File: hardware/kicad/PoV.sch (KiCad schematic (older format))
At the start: 10 parts, among them SW1 SW_DPDT_x2, U1 ATtiny85-20PU

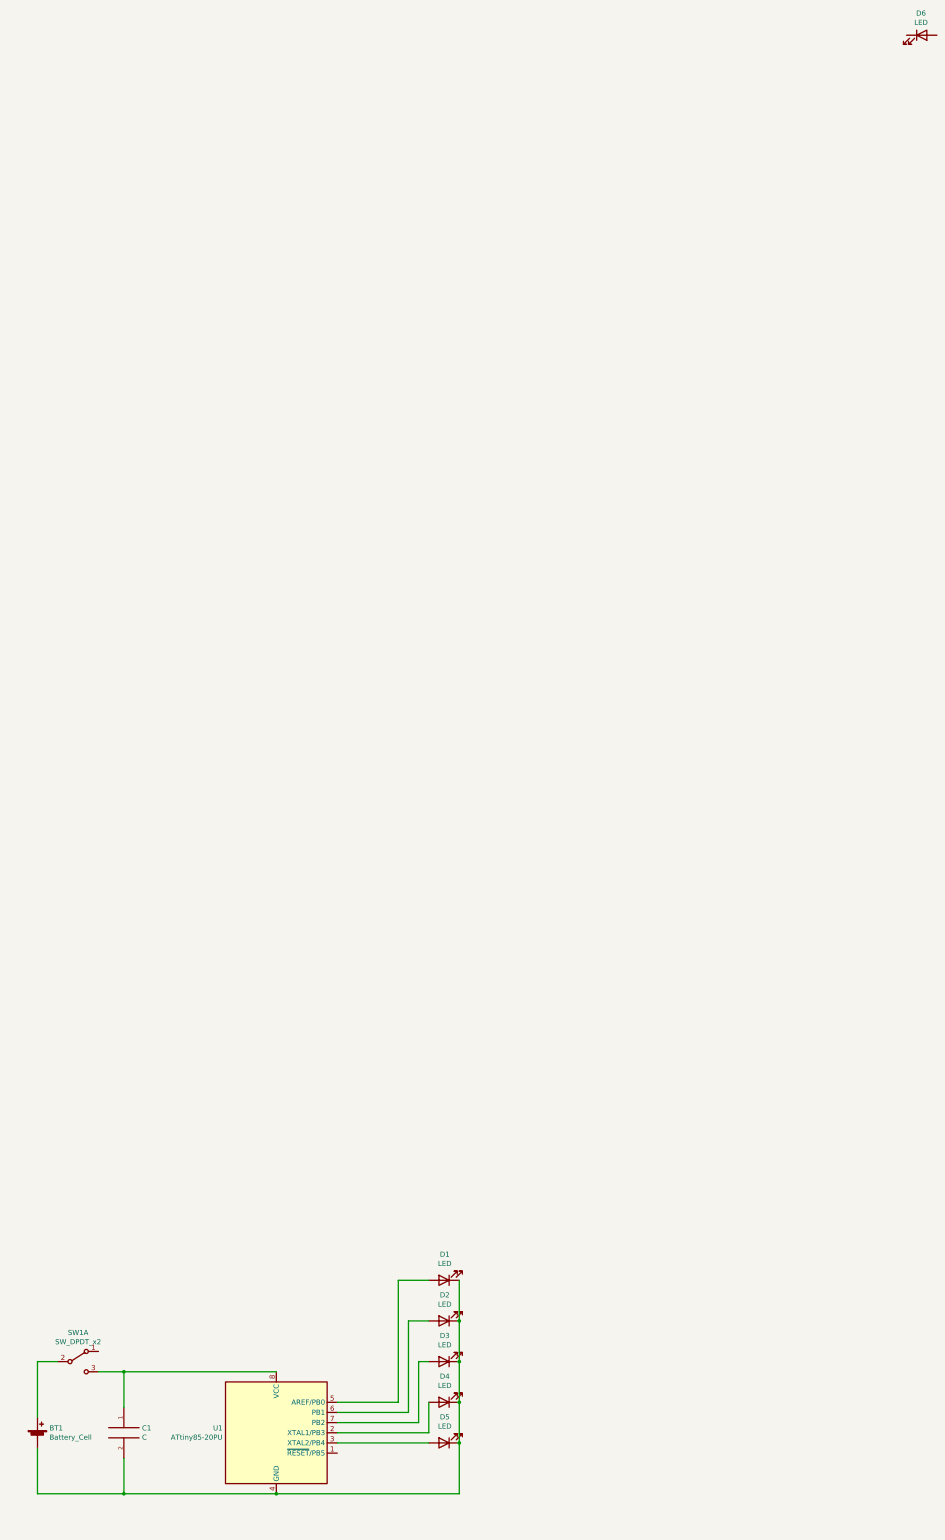
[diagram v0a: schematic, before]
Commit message: updated kicad schematic
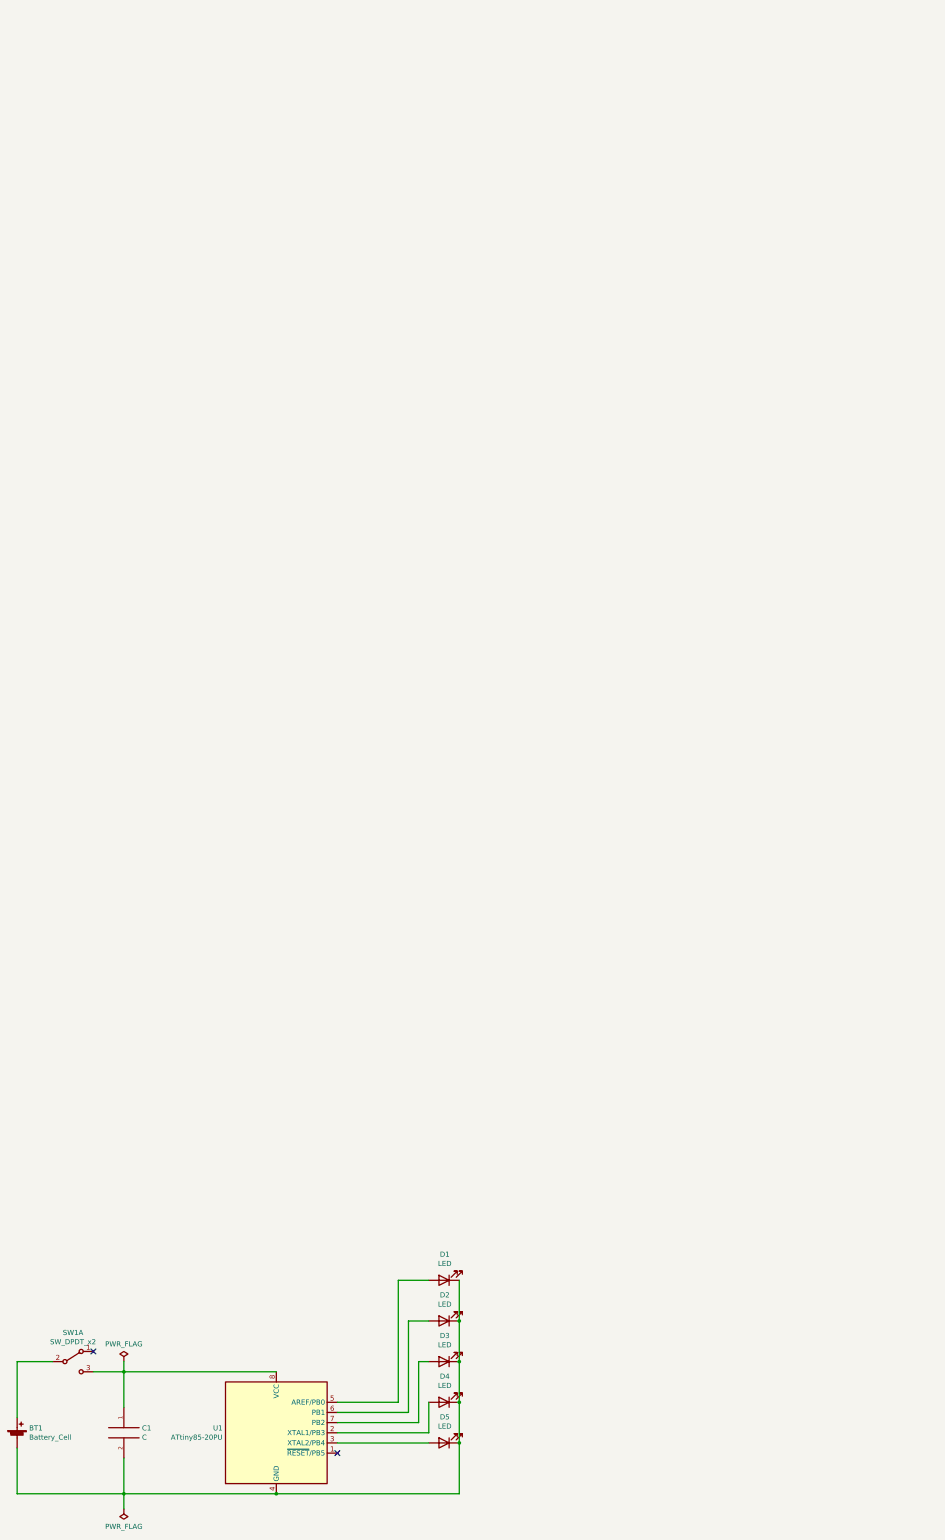
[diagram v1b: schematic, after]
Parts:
- removed D6: LED, symbol Device:LED
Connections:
- no-connect marks 0 -> 2
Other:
- moved on the sheet: BT1, SW1A
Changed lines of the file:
@@
-$EndComp
-$Comp
-L Device:LED D6
-U 1 1 6151B918
-P 12350 -9750
-F 0 "D6" H 12343 -9534 50  0000 C CNN
-F 1 "LED" H 12343 -9625 50  0000 C CNN
-F 2 "" H 12350 -9750 50  0001 C CNN
-F 3 "~" H 12350 -9750 50  0001 C CNN
-	1    12350 -9750
-	1    0    0    -1
 $EndComp
 $Comp
@@
 L Device:Battery_Cell BT1
 U 1 1 61526F5A
-P 3650 4050
-F 0 "BT1" H 3768 4146 50  0000 L CNN
-F 1 "Battery_Cell" H 3768 4055 50  0000 L CNN
-F 2 "" V 3650 4110 50  0001 C CNN
-F 3 "~" V 3650 4110 50  0001 C CNN
-	1    3650 4050
+P 3450 4050
+F 0 "BT1" H 3568 4146 50  0000 L CNN
+F 1 "Battery_Cell" H 3568 4055 50  0000 L CNN
+F 2 "" V 3450 4110 50  0001 C CNN
+F 3 "~" V 3450 4110 50  0001 C CNN
+	1    3450 4050
 	1    0    0    -1
 $EndComp
@@
 Wire Wire Line
 	4500 4600 4500 4250
-Wire Wire Line
-	3650 4150 3650 4600
-Wire Wire Line
-	3650 4600 4500 4600
-Connection ~ 4500 4600
 Wire Wire Line
 	6600 4100 7500 4100
@@
 L Switch:SW_DPDT_x2 SW1
 U 1 1 6154A9DE
-P 4050 3300
-F 0 "SW1" H 4050 3585 50  0000 C CNN
-F 1 "SW_DPDT_x2" H 4050 3494 50  0000 C CNN
-F 2 "" H 4050 3300 50  0001 C CNN
-F 3 "~" H 4050 3300 50  0001 C CNN
-	1    4050 3300
+P 4000 3300
+F 0 "SW1" H 4000 3585 50  0000 C CNN
+F 1 "SW_DPDT_x2" H 4000 3494 50  0000 C CNN
+F 2 "" H 4000 3300 50  0001 C CNN
+F 3 "~" H 4000 3300 50  0001 C CNN
+	1    4000 3300
+	1    0    0    -1
+$EndComp
+Connection ~ 4500 3400
+NoConn ~ 4200 3200
+NoConn ~ 6600 4200
+$Comp
+L power:PWR_FLAG #FLG0101
+U 1 1 6155DBBA
+P 4500 3300
+F 0 "#FLG0101" H 4500 3375 50  0001 C CNN
+F 1 "PWR_FLAG" H 4500 3473 50  0000 C CNN
+F 2 "" H 4500 3300 50  0001 C CNN
+F 3 "~" H 4500 3300 50  0001 C CNN
+	1    4500 3300
 	1    0    0    -1
 $EndComp
 Wire Wire Line
-	3850 3300 3650 3300
+	4500 4600 3450 4600
 Wire Wire Line
-	3650 3300 3650 3850
+	3450 4600 3450 4150
+Connection ~ 4500 4600
 Wire Wire Line
-	4250 3400 4500 3400
-Connection ~ 4500 3400
+	3450 3850 3450 3300
+Wire Wire Line
+	4500 3300 4500 3400
+Wire Wire Line
+	4500 3400 4200 3400
+Wire Wire Line
+	3800 3300 3450 3300
+$Comp
+L power:PWR_FLAG #FLG0102
+U 1 1 6156979C
+P 4500 4750
+F 0 "#FLG0102" H 4500 4825 50  0001 C CNN
+F 1 "PWR_FLAG" H 4500 4923 50  0000 C CNN
+F 2 "" H 4500 4750 50  0001 C CNN
+F 3 "~" H 4500 4750 50  0001 C CNN
+	1    4500 4750
+	-1   0    0    1
+$EndComp
+Wire Wire Line
+	4500 4600 4500 4750
 $EndSCHEMATC

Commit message: woking on kicad
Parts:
- BT1: footprint (none) -> Battery:BatteryHolder_Keystone_103_1x20mm
- C1: footprint (none) -> Capacitor_THT:C_Disc_D3.0mm_W1.6mm_P2.50mm
- D1, D2, D3, D4, D5: footprint (none) -> LED_THT:LED_D5.0mm
- SW1: footprint (none) -> Button_Switch_THT:SW_CuK_JS202011AQN_DPDT_Angled
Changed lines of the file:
@@
 EESchema Schematic File Version 4
+LIBS:PoV-cache
 EELAYER 30 0
 EELAYER END
@@
 F 0 "D1" H 7643 2245 50  0000 C CNN
 F 1 "LED" H 7643 2336 50  0000 C CNN
-F 2 "" H 7650 2500 50  0001 C CNN
+F 2 "LED_THT:LED_D5.0mm" H 7650 2500 50  0001 C CNN
 F 3 "~" H 7650 2500 50  0001 C CNN
 	1    7650 2500
@@
 F 0 "D2" H 7643 2645 50  0000 C CNN
 F 1 "LED" H 7643 2736 50  0000 C CNN
-F 2 "" H 7650 2900 50  0001 C CNN
+F 2 "LED_THT:LED_D5.0mm" H 7650 2900 50  0001 C CNN
 F 3 "~" H 7650 2900 50  0001 C CNN
 	1    7650 2900
@@
 F 0 "D3" H 7643 3045 50  0000 C CNN
 F 1 "LED" H 7643 3136 50  0000 C CNN
-F 2 "" H 7650 3300 50  0001 C CNN
+F 2 "LED_THT:LED_D5.0mm" H 7650 3300 50  0001 C CNN
 F 3 "~" H 7650 3300 50  0001 C CNN
 	1    7650 3300
@@
 F 0 "D4" H 7643 3445 50  0000 C CNN
 F 1 "LED" H 7643 3536 50  0000 C CNN
-F 2 "" H 7650 3700 50  0001 C CNN
+F 2 "LED_THT:LED_D5.0mm" H 7650 3700 50  0001 C CNN
 F 3 "~" H 7650 3700 50  0001 C CNN
 	1    7650 3700
@@
 F 0 "D5" H 7643 3845 50  0000 C CNN
 F 1 "LED" H 7643 3936 50  0000 C CNN
-F 2 "" H 7650 4100 50  0001 C CNN
+F 2 "LED_THT:LED_D5.0mm" H 7650 4100 50  0001 C CNN
 F 3 "~" H 7650 4100 50  0001 C CNN
 	1    7650 4100
@@
 F 0 "BT1" H 3568 4146 50  0000 L CNN
 F 1 "Battery_Cell" H 3568 4055 50  0000 L CNN
-F 2 "" V 3450 4110 50  0001 C CNN
+F 2 "Battery:BatteryHolder_Keystone_103_1x20mm" V 3450 4110 50  0001 C CNN
 F 3 "~" V 3450 4110 50  0001 C CNN
 	1    3450 4050
@@
 F 0 "C1" H 4678 4046 50  0000 L CNN
 F 1 "C" H 4678 3955 50  0000 L CNN
-F 2 "" H 4500 4000 50  0001 C CNN
+F 2 "Capacitor_THT:C_Disc_D3.0mm_W1.6mm_P2.50mm" H 4500 4000 50  0001 C CNN
 F 3 "~" H 4500 4000 50  0001 C CNN
 	1    4500 4000
@@
 F 0 "SW1" H 4000 3585 50  0000 C CNN
 F 1 "SW_DPDT_x2" H 4000 3494 50  0000 C CNN
-F 2 "" H 4000 3300 50  0001 C CNN
+F 2 "Button_Switch_THT:SW_CuK_JS202011AQN_DPDT_Angled" H 4000 3300 50  0001 C CNN
 F 3 "~" H 4000 3300 50  0001 C CNN
 	1    4000 3300

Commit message: added first schematic draw
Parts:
- U1: symbol MCU_Microchip_ATtiny:ATtiny85-20PU -> PoV-rescue:ATtiny85-20PU-MCU_Microchip_ATtiny
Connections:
- net at C1.1, U1.8 (VCC): now also SW1.2 (B); no longer SW1.3 (C)
- net at BT1.1 (+): now also SW1.3 (C); no longer SW1.2 (B)
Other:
- moved on the sheet: SW1A
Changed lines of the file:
@@
 EESchema Schematic File Version 4
-LIBS:PoV-cache
 EELAYER 30 0
 EELAYER END
@@
 $EndDescr
 $Comp
-L MCU_Microchip_ATtiny:ATtiny85-20PU U1
+L PoV-rescue:ATtiny85-20PU-MCU_Microchip_ATtiny U1
 U 1 1 6151AF9F
 P 6000 4000
@@
 L Switch:SW_DPDT_x2 SW1
 U 1 1 6154A9DE
-P 4000 3300
-F 0 "SW1" H 4000 3585 50  0000 C CNN
-F 1 "SW_DPDT_x2" H 4000 3494 50  0000 C CNN
-F 2 "Button_Switch_THT:SW_CuK_JS202011AQN_DPDT_Angled" H 4000 3300 50  0001 C CNN
-F 3 "~" H 4000 3300 50  0001 C CNN
-	1    4000 3300
-	1    0    0    -1
+P 4000 3400
+F 0 "SW1" H 4000 3685 50  0000 C CNN
+F 1 "SW_DPDT_x2" H 4000 3594 50  0000 C CNN
+F 2 "Button_Switch_THT:SW_CuK_JS202011AQN_DPDT_Angled" H 4000 3400 50  0001 C CNN
+F 3 "~" H 4000 3400 50  0001 C CNN
+	1    4000 3400
+	-1   0    0    1
 $EndComp
 Connection ~ 4500 3400
@@
 Wire Wire Line
 	4500 3300 4500 3400
-Wire Wire Line
-	4500 3400 4200 3400
-Wire Wire Line
-	3800 3300 3450 3300
 $Comp
 L power:PWR_FLAG #FLG0102
@@
 Wire Wire Line
 	4500 4600 4500 4750
+Wire Wire Line
+	4200 3400 4500 3400
+Wire Wire Line
+	3450 3300 3800 3300
 $EndSCHEMATC

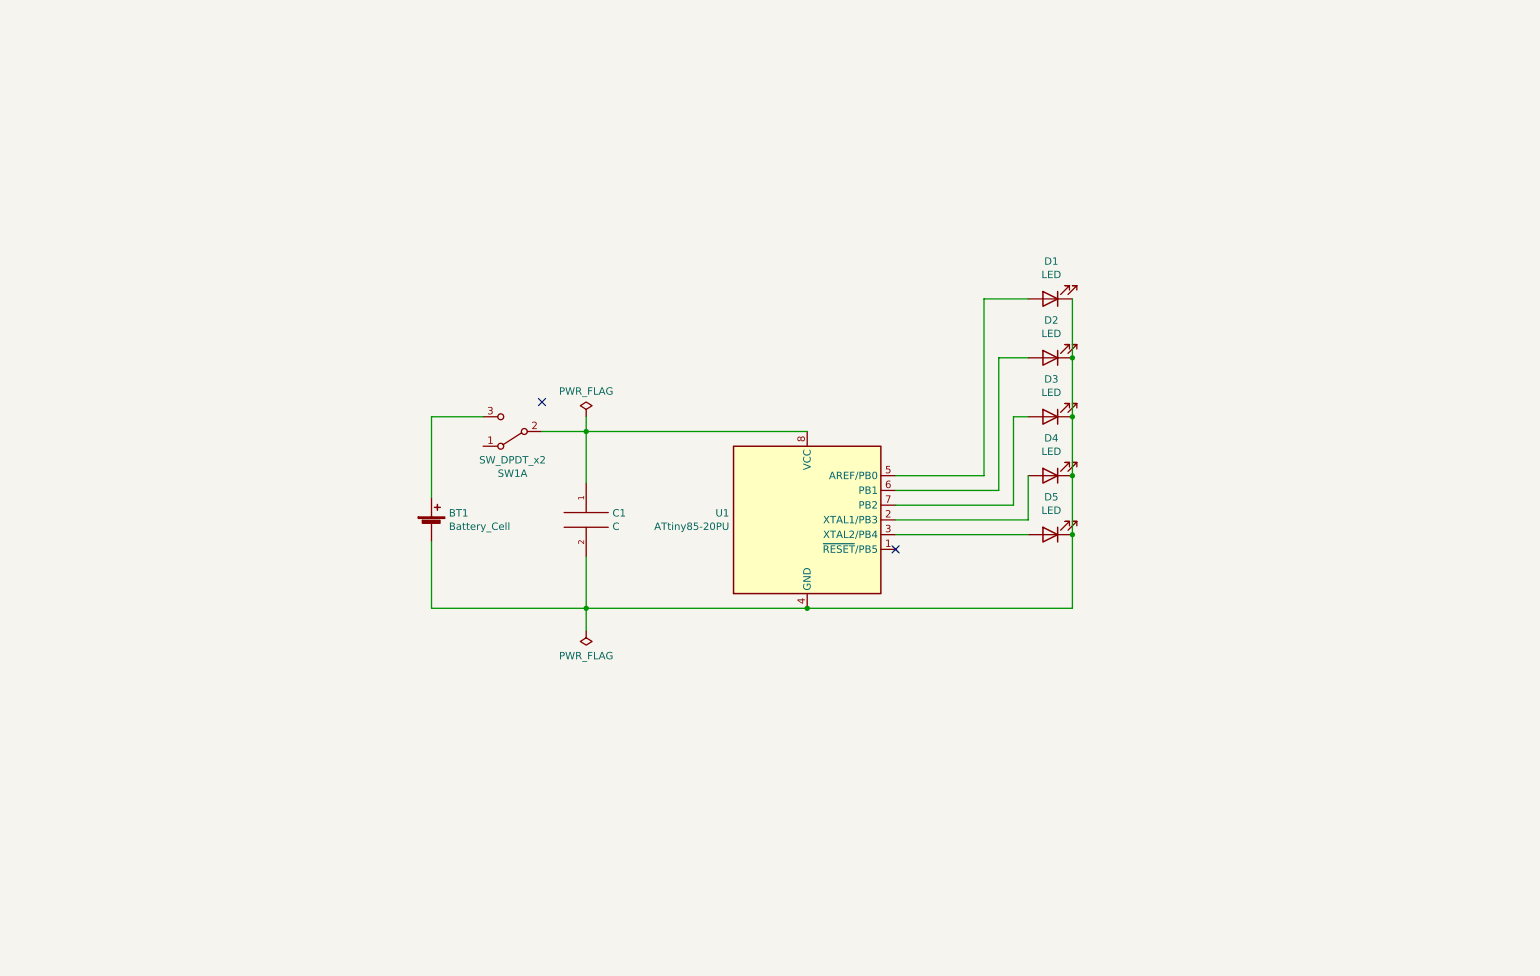
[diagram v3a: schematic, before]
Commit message: now pov is programmable from board
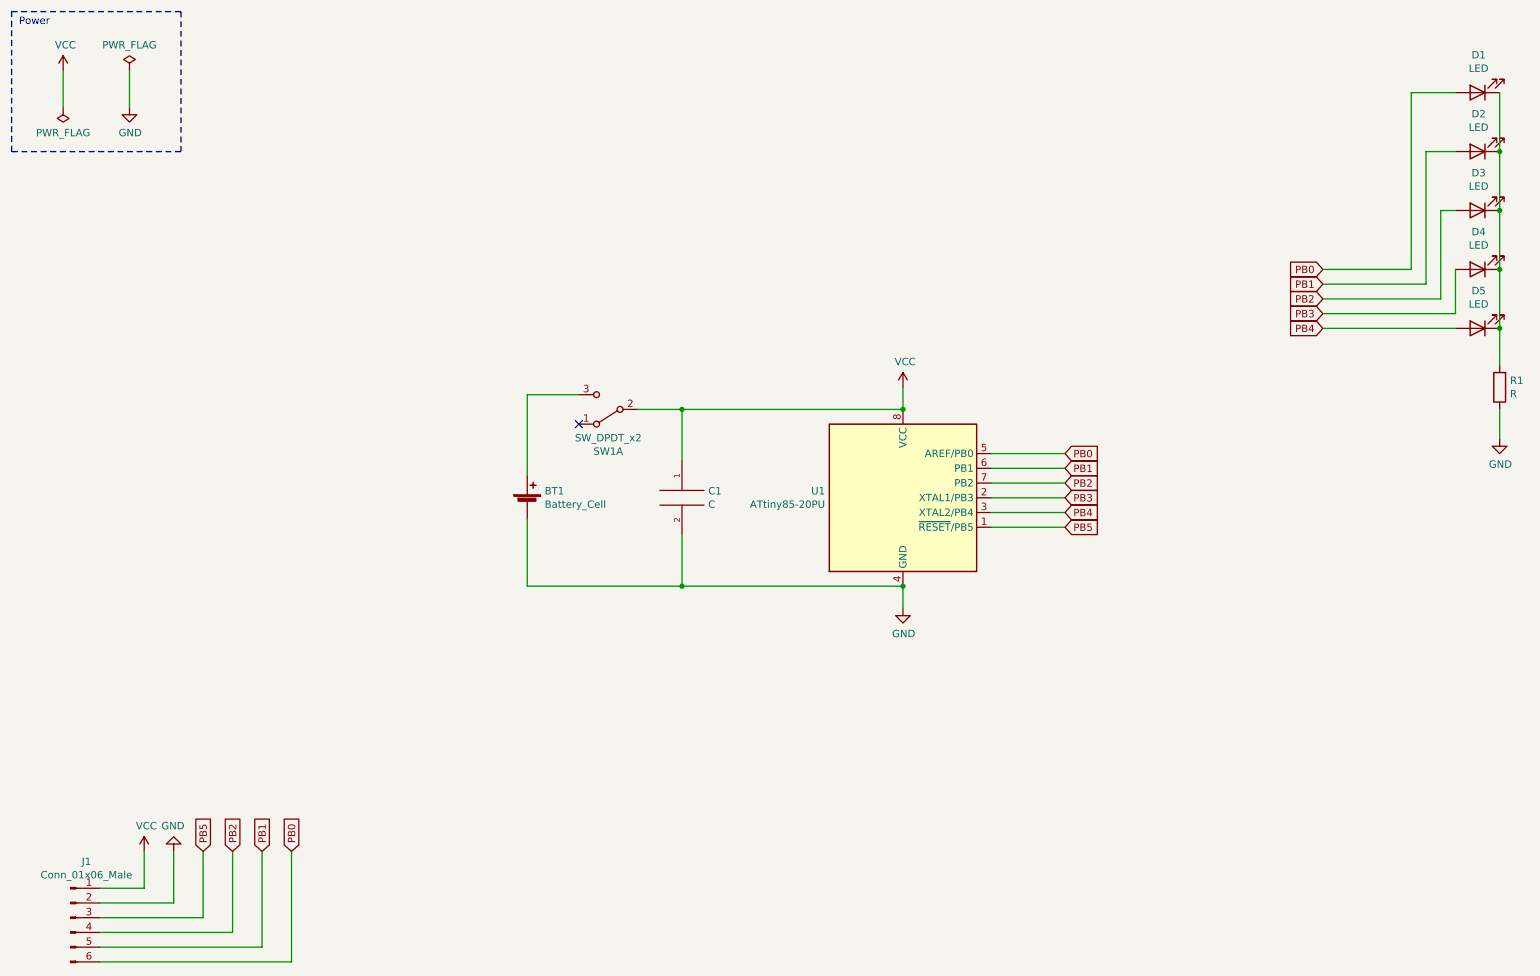
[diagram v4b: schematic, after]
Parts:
- added J1: Conn_01x06_Male, Connector_PinHeader_2.54mm:PinHeader_1x06_P2.54mm_Vertical, symbol Connector:Conn_01x06_Male
- added R1: R, Resistor_THT:R_Axial_DIN0207_L6.3mm_D2.5mm_P7.62mm_Horizontal, symbol Device:R
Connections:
- net PB5: now reaches U1.1 (~RESET~/PB5)
- net PB5: now also J1.3 (Pin_3)
- net PB3: now reaches D4.2 (A), U1.2 (XTAL1/PB3)
- net PB4: now reaches D5.2 (A), U1.3 (XTAL2/PB4)
- net at D1.1 (K), D2.1 (K), D3.1 (K)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: now also R1.2; no longer BT1.2 (-), C1.2, U1.4 (GND)
- net PB0: now reaches D1.2 (A), U1.5 (AREF/PB0)
- net PB0: now also J1.6 (Pin_6)
- net PB1: now reaches D2.2 (A), U1.6 (PB1)
- net PB1: now also J1.5 (Pin_5)
- net PB2: now reaches D3.2 (A), U1.7 (PB2)
- net PB2: now also J1.4 (Pin_4)
- net VCC: now reaches C1.1, SW1.2 (B), U1.8 (VCC)
- net VCC: now also J1.1 (Pin_1)
- new net GND: BT1.2 (-), C1.2, J1.2 (Pin_2), R1.1, U1.4 (GND)
- no-connect marks 2 -> 1
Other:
- note added: "Power"
- moved on the sheet: BT1, C1, D1, D2, D3, D4, D5, SW1A, U1
